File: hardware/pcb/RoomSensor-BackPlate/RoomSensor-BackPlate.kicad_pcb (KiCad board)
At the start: 4 copper layers, 89 x 65 mm, 12 parts, among them SW1 Voltage EX1, SW2 Voltage EX2, U1 PCF8574P

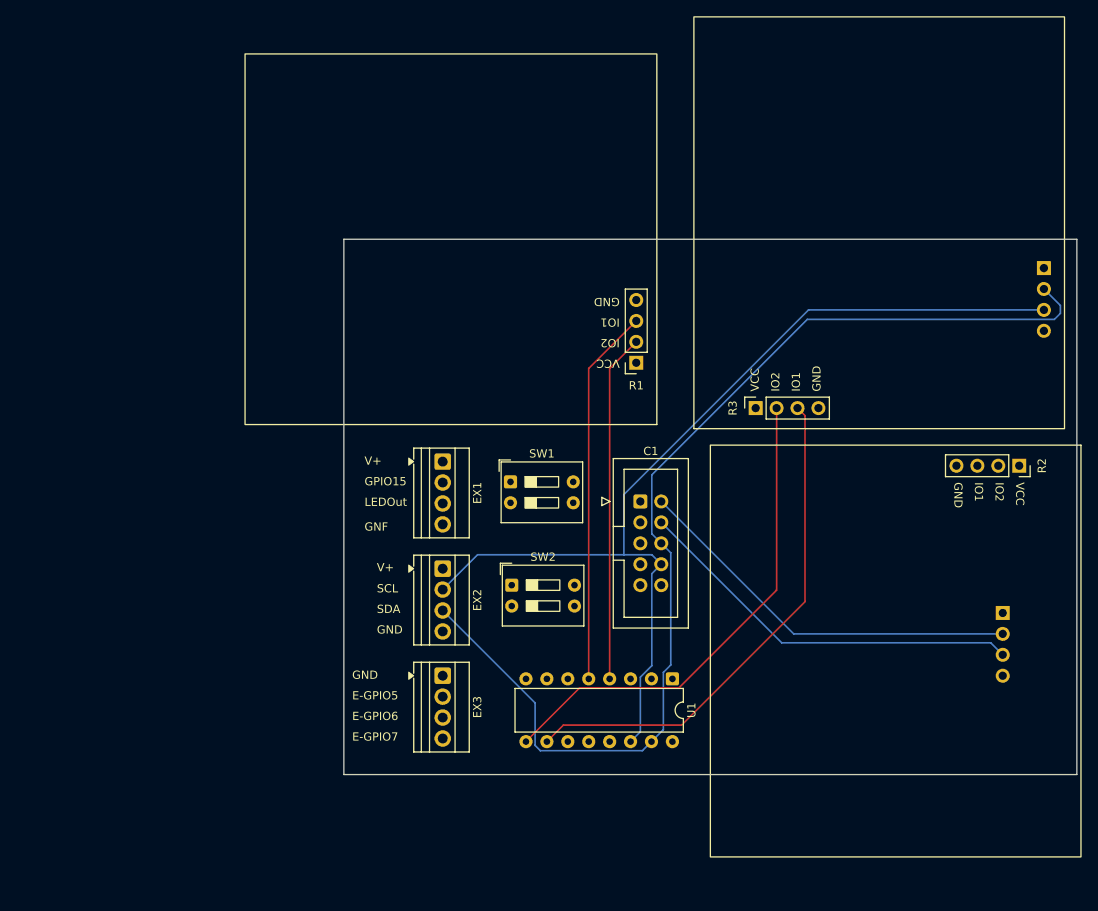
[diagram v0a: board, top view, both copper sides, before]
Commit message: hardware: move footprint/symbol libs into pcb/, update KiCad project settings
Move room-sensor.pretty/ and room-sensor.kicad_sym into hardware/pcb/ so all
PCB design files live under one directory. Also picks up KiCad project edits:
BOM preset config and pin_to_pin ERC rule change to error on both plates.

Co-Authored-By: Claude Sonnet 4.6 <noreply@anthropic.com>
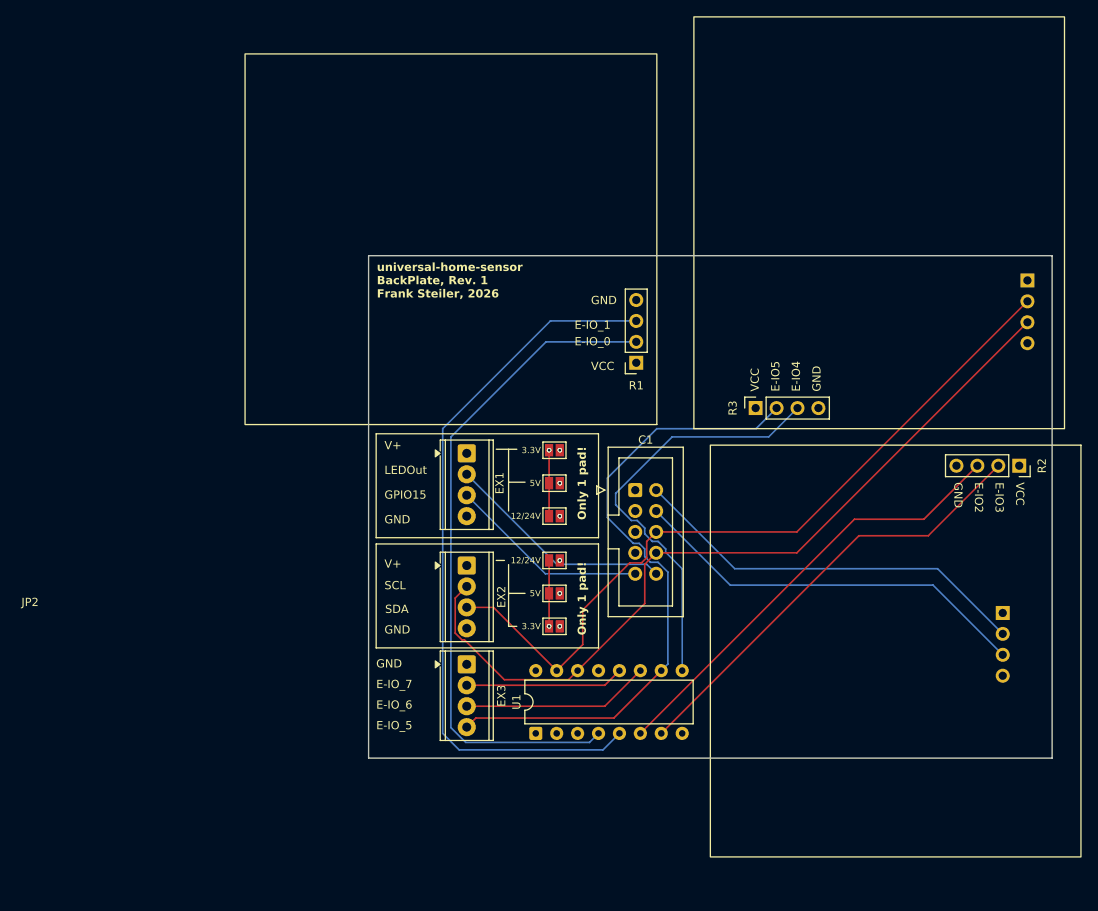
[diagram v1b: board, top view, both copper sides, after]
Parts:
- removed SW1: Voltage EX1, Button_Switch_THT:SW_DIP_SPSTx02_Slide_9.78x7.26mm_W7.62mm_P2.54mm
- removed SW2: Voltage EX2, Button_Switch_THT:SW_DIP_SPSTx02_Slide_9.78x7.26mm_W7.62mm_P2.54mm
- added JP1: SolderJumper_2_Open, Jumper:SolderJumper-2_P1.3mm_Open_Pad1.0x1.5mm, F.Cu at (118.6, 109.0)
- added JP2: SolderJumper_2_Open, Jumper:SolderJumper-2_P1.3mm_Open_Pad1.0x1.5mm, F.Cu at (118.6, 105.0)
- added JP3: SolderJumper_2_Open, Jumper:SolderJumper-2_P1.3mm_Open_Pad1.0x1.5mm, F.Cu at (118.6, 101.0)
- added JP4: SolderJumper_2_Open, Jumper:SolderJumper-2_P1.3mm_Open_Pad1.0x1.5mm, F.Cu at (118.6, 87.6)
- added JP5: SolderJumper_2_Open, Jumper:SolderJumper-2_P1.3mm_Open_Pad1.0x1.5mm, F.Cu at (118.6, 91.6)
- added JP6: SolderJumper_2_Open, Jumper:SolderJumper-2_P1.3mm_Open_Pad1.0x1.5mm, F.Cu at (118.6, 95.6)
- EX1, EX2, EX3: footprint TerminalBlock:TerminalBlock_Xinya_XY308-2.54-4P_1x04_P2.54mm_Horizontal -> TerminalBlock_Phoenix:TerminalBlock_Phoenix_MPT-0,5-4-2.54_1x04_P2.54mm_Horizontal
- moved U1 17.9 mm to (116.3, 122.0), turned to 90 degrees
- moved EX3 3.23 mm to (107.9, 113.6)
- moved EX1 3.09 mm to (107.9, 88.0)
- moved EX2 2.94 mm to (107.9, 101.6)
- moved L1 2.50 mm to (176.0, 67.0)
- moved C1 1.51 mm to (128.4, 92.5)
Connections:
- net Net-(EX3-E_GPIO6) renamed /E-GPIO6
- net Net-(R1-IO1) renamed /E-GPIO1
- net Net-(R1-IO2) renamed /E-GPIO0
- EX1 pad 2: /GPIO15 -> /LED Bus
- EX1 pad 3: /LED Bus -> /GPIO15
- EX3 pad 2: Net-(EX3-E-GPIO5) -> /E-GPIO7
- EX3 pad 4: Net-(EX3-E_GPIO7) -> /E-GPIO5
- R2 pad 2: Net-(R2-IO2) -> /E-GPIO3
- R2 pad 3: Net-(R2-IO1) -> /E-GPIO2
- R3 pad 2: Net-(R3-IO2) -> /E-GPIO5
- R3 pad 3: Net-(EX3-E-GPIO5) -> /E-GPIO4
- U1 pad 10: Net-(EX3-E-GPIO5) -> /E-GPIO5
- U1 pad 12: Net-(EX3-E_GPIO7) -> /E-GPIO7
- U1 pad 6: Net-(R2-IO2) -> /E-GPIO2
- U1 pad 7: Net-(R2-IO1) -> /E-GPIO3
- U1 pad 9: Net-(R3-IO2) -> /E-GPIO4
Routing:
- net /E-GPIO5: track 0.00 -> 78.2 mm
- net Net-(EX3-E-GPIO5): track 77.2 -> 0.00 mm
- net Net-(C1-SDA): track 168.7 -> 93.5 mm
- net Net-(R2-IO2): track 63.0 -> 0.00 mm
- net Net-(R2-IO1): track 63.0 -> 0.00 mm
- net Net-(R3-IO2): track 60.2 -> 0.00 mm
- net Net-(C1-SCL): track 153.5 -> 98.8 mm
- net /E-GPIO3: track 0.00 -> 54.4 mm
- net /E-GPIO2: track 0.00 -> 54.4 mm
- net /E-GPIO4: track 0.00 -> 52.1 mm
- net /E-GPIO1: track 45.9 -> 89.0 mm
- net /E-GPIO0: track 42.3 -> 81.7 mm
- net /E-GPIO7: track 0.00 -> 19.3 mm
- net Net-(EX3-E_GPIO7): track 19.1 -> 0.00 mm
- net /GND: track 267.8 -> 282.6 mm
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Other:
- board size 89 x 65 mm -> 83 x 61 mm
- board text added: "12/24V"
- board text added: "3.3V"
- board text added: "5V"
- board text added: "E-IO_5"
- board text added: "E-IO_6"
- board text added: "E-IO_7"
- board text added: "EX1"
- board text added: "GND"
- board text added: "GPIO15"
- board text added: "LEDOut"
- board text added: "Only 1 pad!"
- board text added: "SCL"
- board text added: "SDA"
- board text added: "V+"
- board text added: "universal-home-sensor BackPlate, Rev. 1 Frank Steiler, 2026"

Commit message: hardware: back plate mounting holes + EX2 routing, plot settings cleanup
BackPlate: add four M3 mounting holes, re-place EX2 (I2S External) and
route the remaining nets (+26 track segments, 7 new schematic wires).
MainPlate: switch plot output to a repo-relative directory instead of a
local Desktop path, add board outline/keepout drawings.

Co-Authored-By: Claude Opus 5 (1M context) <noreply@anthropic.com>
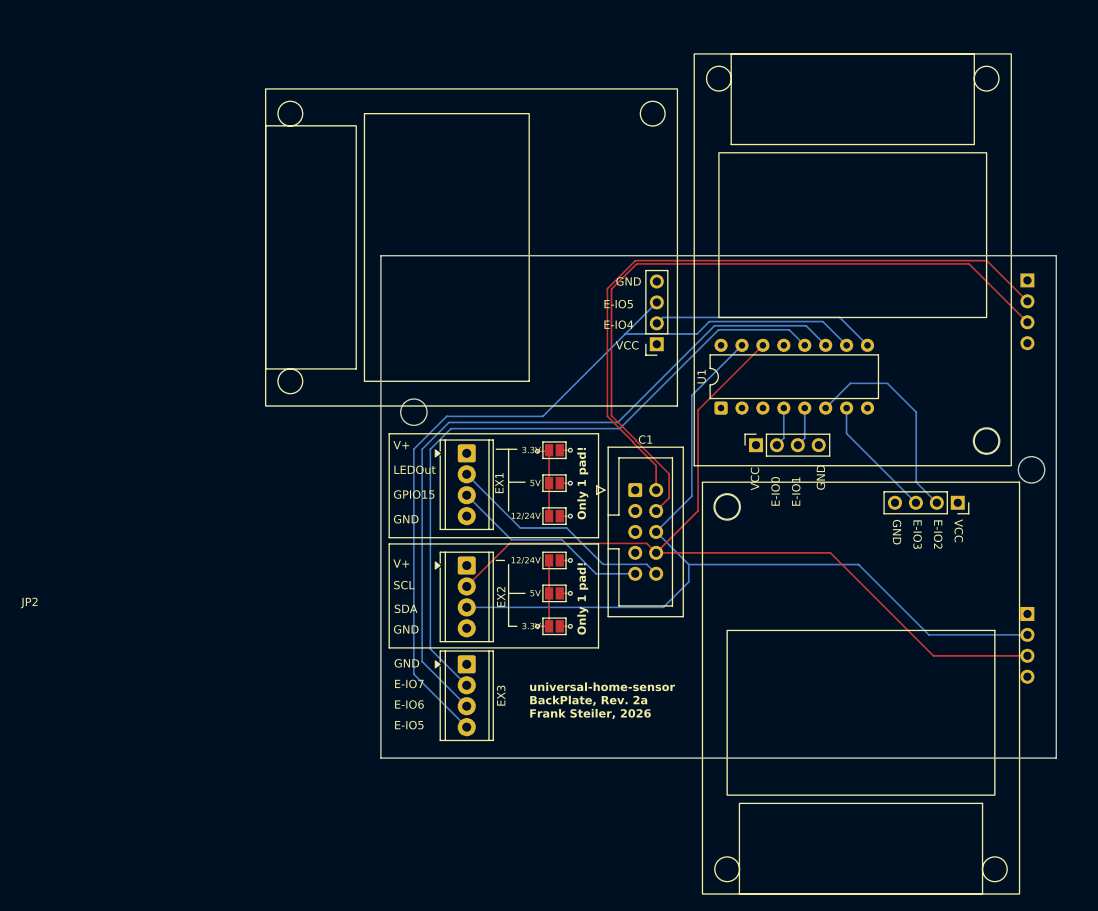
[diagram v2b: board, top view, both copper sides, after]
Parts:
- added REF**: MountingHole_3.2mm_M3, MountingHole:MountingHole_3.2mm_M3, F.Cu at (139.5, 94.5)
- added REF**: MountingHole_3.2mm_M3, MountingHole:MountingHole_3.2mm_M3, F.Cu at (171.0, 86.5)
- added REF**: MountingHole_3.2mm_M3, MountingHole:MountingHole_3.2mm_M3, F.Cu at (176.5, 90.0)
- added REF**: MountingHole_3.2mm_M3, MountingHole:MountingHole_3.2mm_M3, F.Cu at (101.5, 83.0)
- moved U1 45.5 mm to (138.8, 82.5)
- moved L1 40.5 mm to (176.0, 107.5)
- moved E1 40.5 mm to (176.0, 67.0)
- moved R2 8.71 mm to (167.5, 94.0)
- moved R3 4.50 mm to (143.0, 87.0)
- moved R1 3.36 mm to (131.0, 74.8)
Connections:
- R1 pad 2: /E-GPIO0 -> /E-GPIO4
- R1 pad 3: /E-GPIO1 -> /E-GPIO5
- R2 pad 2: /E-GPIO3 -> /E-GPIO2
- R2 pad 3: /E-GPIO2 -> /E-GPIO3
- R3 pad 2: /E-GPIO5 -> /E-GPIO0
- R3 pad 3: /E-GPIO4 -> /E-GPIO1
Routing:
- net /GND: track 282.6 -> 168.2 mm
- net /E-GPIO1: track 89.0 -> 4.85 mm
- net /E-GPIO0: track 81.7 -> 4.85 mm
- net /E-GPIO6: track 22.9 -> 89.6 mm
- net /E-GPIO7: track 19.3 -> 82.7 mm
- net /E-GPIO3: track 54.4 -> 15.0 mm
- net Net-(C1-Energy_TX): track 49.3 -> 85.2 mm
- net Net-(C1-Energy_RX): track 49.3 -> 81.4 mm
- net /+5V: track 197.4 -> 167.0 mm
- net /E-GPIO2: track 54.4 -> 26.3 mm
- net /E-GPIO4: track 52.1 -> 27.3 mm
- net /E-GPIO5: track 78.2 -> 102.1 mm
- net Net-(C1-SDA): track 93.5 -> 107.6 mm
- net Net-(C1-SCL): track 98.8 -> 106.5 mm
- net Net-(C1-+3.3V): track 37.7 -> 41.3 mm
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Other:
- board size 83 x 61 mm -> 82 x 61 mm
- board text added: "10x10mm"
- board text added: "E-IO5"
- board text added: "E-IO6"
- board text added: "E-IO7"
- board text added: "universal-home-sensor BackPlate, Rev. 2a Frank Steiler, 2026"
- board text removed: "E-IO_5"
- board text removed: "E-IO_6"
- board text removed: "E-IO_7"
- board text removed: "universal-home-sensor BackPlate, Rev. 1 Frank Steiler, 2026"
